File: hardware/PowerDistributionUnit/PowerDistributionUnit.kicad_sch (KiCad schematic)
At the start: 95 parts, among them J1 973582101, J2 973582100, J3 973582101, J4 973582100, Q16 CSD18511Q5A, SW1 SW_Push, U1 TPS25983, U2 AD5258, U3 NUCLEO_LK43C

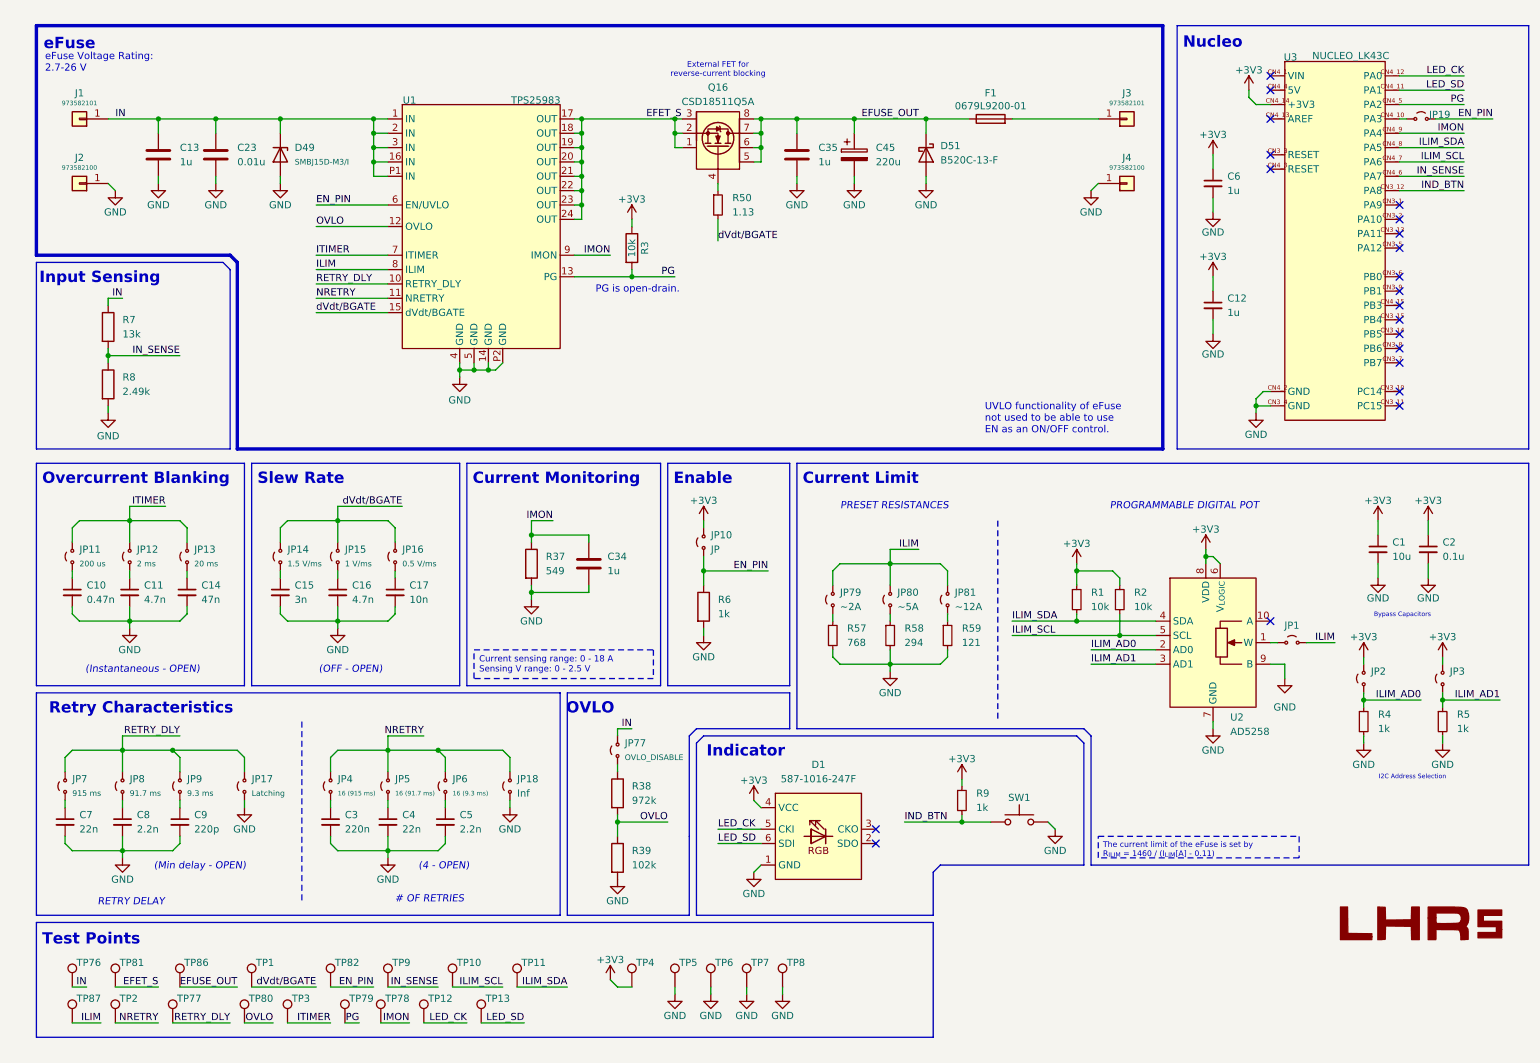
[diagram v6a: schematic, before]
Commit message: added rev polarity protection circuit
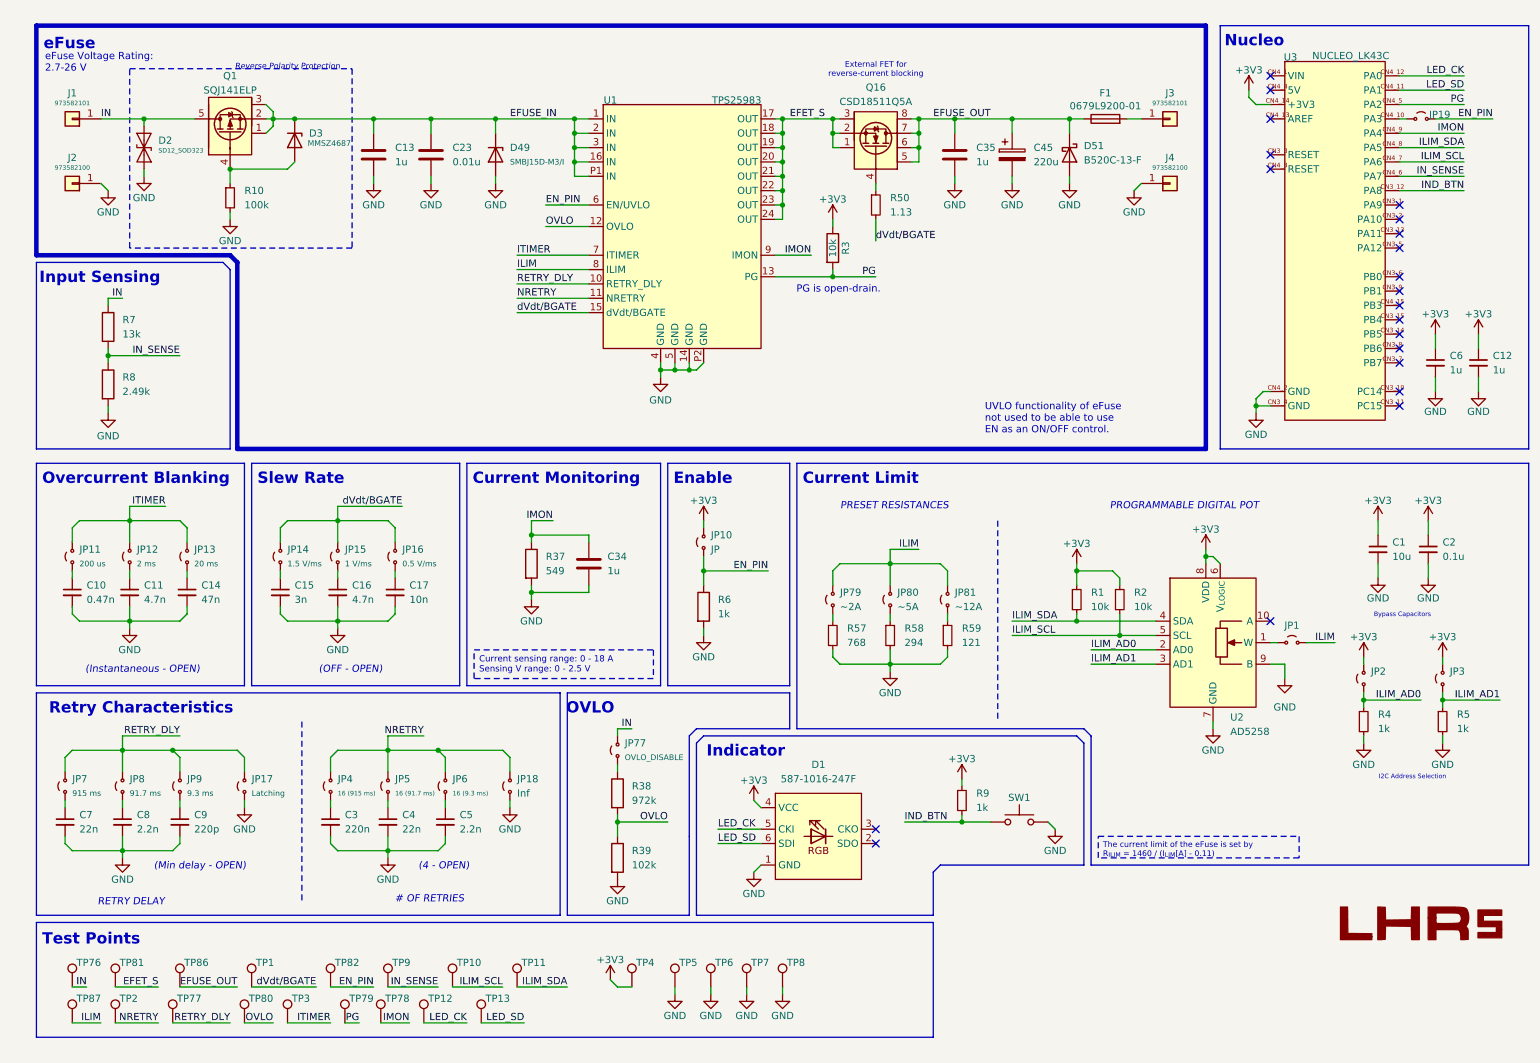
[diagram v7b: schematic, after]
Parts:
- added D2: SD12_SOD323, Diode_SMD:D_SOD-323, symbol Diode:SD12_SOD323
- added D3: MMSZ4687, Diode_SMD:D_SOD-123, symbol Device:D_Zener
- added Q1: SQJ141ELP, Package_SO:PowerPAK_SO-8L_Single, symbol PowerDistributionUnitLib:SQJ141ELP
- added R10: 100k, symbol Device:R_Small
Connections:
- net GND: now also D2.1 (A1), R10.2
- net IN: now also D2.2 (A2), Q1.5; no longer C13.1, C23.1, D49.1 (K), U1.1 (IN), U1.16 (IN), U1.2 (IN), U1.3 (IN), U1.P1 (IN)
- new net: D3.2 (A), Q1.4, R10.1
- new net EFUSE_IN: C13.1, C23.1, D3.1 (K), D49.1 (K), Q1.1, Q1.2, Q1.3, U1.1 (IN), U1.16 (IN), U1.2 (IN), U1.3 (IN), U1.P1 (IN)
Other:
- note added: "Reverse Polarity Protection"
- moved on the sheet: C12, C13, C23, C35, C45, C6, D49, D51, F1, J1, J2, J3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

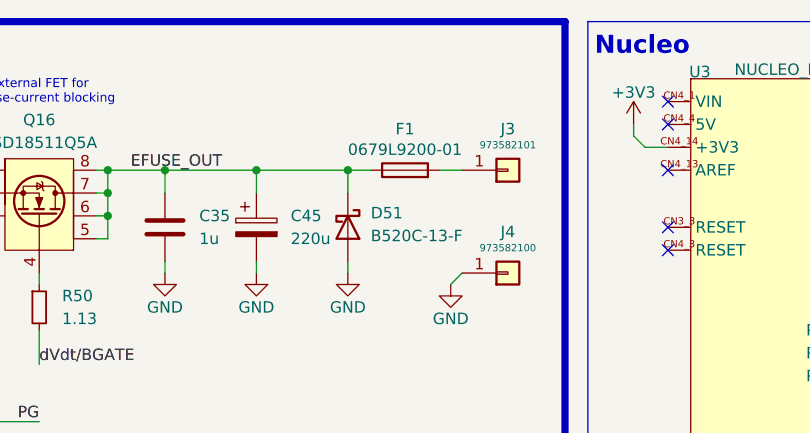
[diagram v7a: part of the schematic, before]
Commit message: changed fuse to blade type
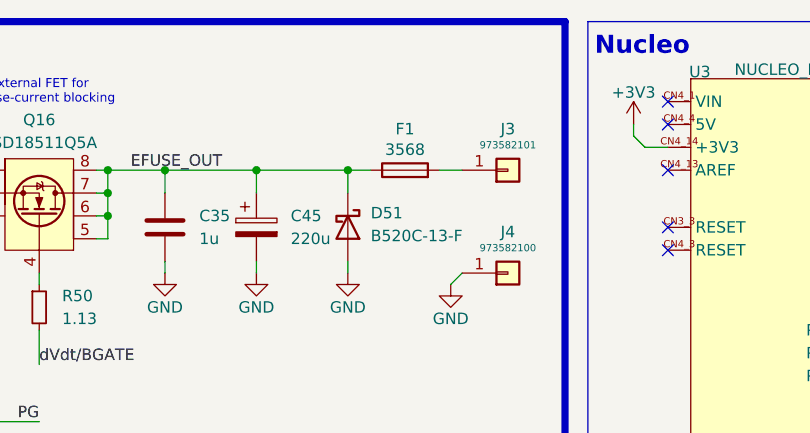
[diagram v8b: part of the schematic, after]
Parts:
- F1: value 0679L9200-01 -> 3568; footprint (none) -> Fuse:Fuseholder_Blade_Mini_Keystone_3568
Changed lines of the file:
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@@
 			)
 		)
-		(property "Value" "0679L9200-01"
+		(property "Value" "3568"
 			(at 205.74 29.464 90)
 			(effects
@@
 			)
 		)
-		(property "Footprint" ""
+		(property "Footprint" "Fuse:Fuseholder_Blade_Mini_Keystone_3568"
 			(at 205.74 33.528 90)
 			(effects
